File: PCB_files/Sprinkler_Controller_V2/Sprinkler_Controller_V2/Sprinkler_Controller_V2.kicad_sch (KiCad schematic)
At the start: 42 parts, among them J1 Screw_Terminal_01x02, J2 Screw_Terminal_01x11, U1 ESP32_DevKit_V1_DOIT, U12 TPP362081-T6TR

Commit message: V2 PCB Complete
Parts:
- added SW1: SW_SPST, Connector_PinHeader_2.54mm:PinHeader_1x02_P2.54mm_Vertical, symbol Switch:SW_SPST
- L1: footprint (none) -> Inductor_SMD:L_Vishay_IHLP-5050
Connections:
- net AC: now also SW1.2 (B); no longer J1.1 (Pin_1)
- new net AC_to_SW: J1.1 (Pin_1), SW1.1 (A)
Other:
- moved on the sheet: J1
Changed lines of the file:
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@@
 	)
 	(junction
-		(at 20.32 22.86)
-		(diameter 0)
-		(color 0 0 0 0)
-	)
-	(junction
 		(at 45.72 27.94)
 		(diameter 0)
@@
 	)
 	(junction
+		(at 25.4 27.94)
+		(diameter 0)
+		(color 0 0 0 0)
+	)
+	(junction
 		(at 35.56 43.18)
 		(diameter 0)
@@
 	(wire
 		(pts
+			(xy 19.05 22.86) (xy 19.05 25.4)
+		)
+		(stroke
+			(width 0)
+			(type default)
+		)
+	)
+	(wire
+		(pts
 			(xy 146.05 109.22) (xy 146.05 96.52)
 		)
@@
 	(wire
 		(pts
-			(xy 12.7 15.24) (xy 12.7 29.21)
+			(xy 12.7 15.24) (xy 12.7 40.64)
 		)
 		(stroke
@@
 	(wire
 		(pts
+			(xy 20.32 24.13) (xy 24.13 24.13)
+		)
+		(stroke
+			(width 0)
+			(type default)
+		)
+	)
+	(wire
+		(pts
 			(xy 153.67 129.54) (xy 175.26 129.54)
 		)
@@
 	(wire
 		(pts
+			(xy 20.32 22.86) (xy 20.32 24.13)
+		)
+		(stroke
+			(width 0)
+			(type default)
+		)
+	)
+	(wire
+		(pts
 			(xy 146.05 125.73) (xy 156.21 125.73)
 		)
@@
 	(wire
 		(pts
+			(xy 19.05 25.4) (xy 15.24 25.4)
+		)
+		(stroke
+			(width 0)
+			(type default)
+		)
+	)
+	(wire
+		(pts
 			(xy 219.71 99.06) (xy 219.71 158.75)
 		)
@@
 	(wire
 		(pts
+			(xy 19.05 20.32) (xy 20.32 20.32)
+		)
+		(stroke
+			(width 0)
+			(type default)
+		)
+	)
+	(wire
+		(pts
 			(xy 243.84 93.98) (xy 214.63 93.98)
 		)
@@
 	(wire
 		(pts
+			(xy 24.13 26.67) (xy 25.4 26.67)
+		)
+		(stroke
+			(width 0)
+			(type default)
+		)
+	)
+	(wire
+		(pts
 			(xy 151.13 21.59) (xy 153.67 21.59)
 		)
@@
 	(wire
 		(pts
+			(xy 24.13 24.13) (xy 24.13 26.67)
+		)
+		(stroke
+			(width 0)
+			(type default)
+		)
+	)
+	(wire
+		(pts
 			(xy 133.35 109.22) (xy 146.05 109.22)
 		)
@@
 	(wire
 		(pts
+			(xy 15.24 25.4) (xy 15.24 27.94)
+		)
+		(stroke
+			(width 0)
+			(type default)
+		)
+	)
+	(wire
+		(pts
 			(xy 153.67 115.57) (xy 153.67 129.54)
 		)
@@
 	(wire
 		(pts
+			(xy 25.4 26.67) (xy 25.4 27.94)
+		)
+		(stroke
+			(width 0)
+			(type default)
+		)
+	)
+	(wire
+		(pts
 			(xy 209.55 86.36) (xy 209.55 83.82)
 		)
@@
 	(wire
 		(pts
-			(xy 20.32 29.21) (xy 20.32 22.86)
-		)
-		(stroke
-			(width 0)
-			(type default)
-		)
-	)
-	(wire
-		(pts
 			(xy 109.22 121.92) (xy 109.22 119.38)
 		)
@@
 	(wire
 		(pts
+			(xy 25.4 27.94) (xy 25.4 40.64)
+		)
+		(stroke
+			(width 0)
+			(type default)
+		)
+	)
+	(wire
+		(pts
 			(xy 43.18 43.18) (xy 48.26 43.18)
 		)
@@
 	(wire
 		(pts
-			(xy 12.7 29.21) (xy 20.32 29.21)
+			(xy 12.7 40.64) (xy 25.4 40.64)
 		)
 		(stroke
@@
 		)
 	)
+	(global_label "AC_to_SW"
+		(shape input)
+		(at 15.24 27.94 270)
+		(fields_autoplaced yes)
+		(effects
+			(font
+				(size 1.27 1.27)
+			)
+			(justify right)
+		)
+		(property "Intersheetrefs" "${INTERSHEET_REFS}"
+			(at 15.24 39.7546 90)
+			(effects
+				(font
+					(size 1.27 1.27)
+				)
+				(justify right)
+				(hide yes)
+			)
+		)
+	)
 	(global_label "FB"
 		(shape input)
@@
 	)
 	(symbol
+		(lib_id "Switch:SW_SPST")
+		(at 20.32 27.94 0)
+		(unit 1)
+		(exclude_from_sim no)
+		(in_bom yes)
+		(on_board yes)
+		(dnp no)
+		(property "Reference" "SW1"
+			(at 18.034 25.4 0)
+			(effects
+				(font
+					(size 1.27 1.27)
+				)
+			)
+		)
+		(property "Value" "SW_SPST"
+			(at 20.32 30.48 0)
+			(effects
+				(font
+					(size 1.27 1.27)
+				)
+			)
+		)
+		(property "Footprint" "Connector_PinHeader_2.54mm:PinHeader_1x02_P2.54mm_Vertical"
+			(at 20.32 27.94 0)
+			(effects
+				(font
+					(size 1.27 1.27)
+				)
+				(hide yes)
+			)
+		)
+		(property "Datasheet" "~"
+			(at 20.32 27.94 0)
+			(effects
+				(font
+					(size 1.27 1.27)
+				)
+				(hide yes)
+			)
+		)
+		(property "Description" "Single Pole Single Throw (SPST) switch"
+			(at 20.32 27.94 0)
+			(effects
+				(font
+					(size 1.27 1.27)
+				)
+				(hide yes)
+			)
+		)
+		(pin "1"
+		)
+		(pin "2"
+		)
+		(instances
+			(project ""
+				(path "/4ebb9756-e934-4387-ad3a-d5db36981b1a"
+					(reference "SW1")
+					(unit 1)
+				)
+			)
+		)
+	)
+	(symbol
 		(lib_id "Device:LED")
 		(at 160.02 49.53 180)
@@
 			)
 		)
-		(property "Footprint" ""
+		(property "Footprint" "Inductor_SMD:L_Vishay_IHLP-5050"
 			(at 39.37 43.18 0)
 			(effects
@@
 	(symbol
 		(lib_id "Connector:Screw_Terminal_01x02")
-		(at 15.24 22.86 180)
+		(at 13.97 22.86 180)
 		(unit 1)
 		(exclude_from_sim no)
@@
 		(dnp no)
 		(property "Reference" "J1"
-			(at 16.002 26.162 0)
+			(at 14.732 26.162 0)
 			(effects
 				(font
@@
 		)
 		(property "Value" "Screw_Terminal_01x02"
-			(at 35.052 15.748 0)
+			(at 33.782 15.748 0)
 			(effects
 				(font
@@
 		)
 		(property "Footprint" "TerminalBlock_MetzConnect:TerminalBlock_MetzConnect_Type094_RT03502HBLU_1x02_P5.00mm_Horizontal"
-			(at 15.24 22.86 0)
+			(at 13.97 22.86 0)
 			(effects
 				(font
@@
 		)
 		(property "Datasheet" "~"
-			(at 15.24 22.86 0)
+			(at 13.97 22.86 0)
 			(effects
 				(font
@@
 		)
 		(property "Description" "Generic screw terminal, single row, 01x02, script generated (kicad-library-utils/schlib/autogen/connector/)"
-			(at 15.24 22.86 0)
+			(at 13.97 22.86 0)
 			(effects
 				(font

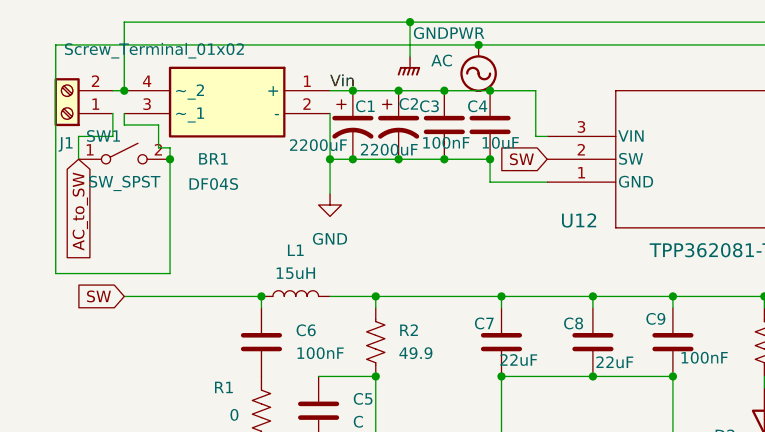
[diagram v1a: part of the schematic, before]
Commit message: changed C1,C2 capacitor values
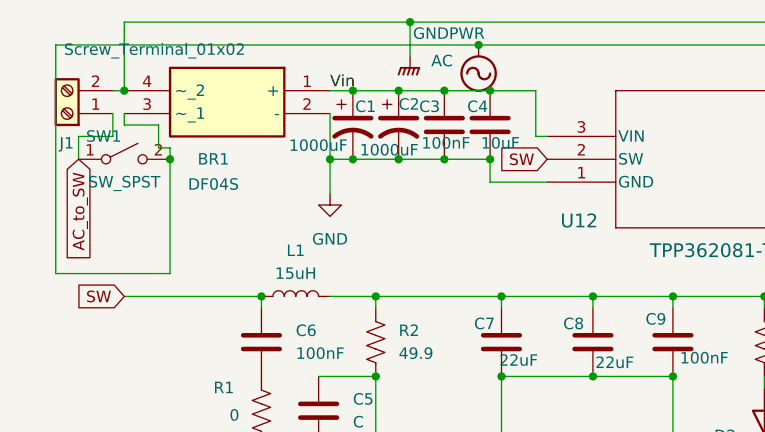
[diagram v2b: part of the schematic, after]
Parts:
- C1, C2: value 2200uF -> 1000uF
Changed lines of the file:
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@@
 			)
 		)
-		(property "Value" "2200uF"
+		(property "Value" "1000uF"
 			(at 46.482 26.924 0)
 			(effects
@@
 			)
 		)
-		(property "Value" "2200uF"
+		(property "Value" "1000uF"
 			(at 38.608 26.416 0)
 			(effects

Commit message: updated size of leds on pcb
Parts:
- D10, D11, D12, D3, D4, D5, D6, D7, D8, D9: footprint LED_SMD:LED_0402_1005Metric -> LED_SMD:LED_0805_2012Metric_Pad1.15x1.40mm_HandSolder
- D2: footprint LED_SMD:LED_0402_1005Metric -> LED_SMD:LED_0805_2012Metric
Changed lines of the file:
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@@
 	(label "Vin"
 		(at 43.18 20.32 0)
-		(fields_autoplaced yes)
 		(effects
 			(font
@@
 			)
 		)
-		(property "Footprint" "LED_SMD:LED_0402_1005Metric"
+		(property "Footprint" "LED_SMD:LED_0805_2012Metric_Pad1.15x1.40mm_HandSolder"
 			(at 158.75 154.94 0)
 			(effects
@@
 			)
 		)
-		(property "Footprint" "LED_SMD:LED_0402_1005Metric"
+		(property "Footprint" "LED_SMD:LED_0805_2012Metric"
 			(at 91.44 57.15 0)
 			(effects
@@
 			)
 		)
-		(property "Footprint" "LED_SMD:LED_0402_1005Metric"
+		(property "Footprint" "LED_SMD:LED_0805_2012Metric_Pad1.15x1.40mm_HandSolder"
 			(at 160.02 96.52 0)
 			(effects
@@
 			)
 		)
-		(property "Footprint" "LED_SMD:LED_0402_1005Metric"
+		(property "Footprint" "LED_SMD:LED_0805_2012Metric_Pad1.15x1.40mm_HandSolder"
 			(at 165.1 35.56 0)
 			(effects
@@
 			)
 		)
-		(property "Footprint" "LED_SMD:LED_0402_1005Metric"
+		(property "Footprint" "LED_SMD:LED_0805_2012Metric_Pad1.15x1.40mm_HandSolder"
 			(at 162.56 64.77 0)
 			(effects
@@
 			)
 		)
-		(property "Footprint" "LED_SMD:LED_0402_1005Metric"
+		(property "Footprint" "LED_SMD:LED_0805_2012Metric_Pad1.15x1.40mm_HandSolder"
 			(at 160.02 49.53 0)
 			(effects
@@
 			)
 		)
-		(property "Footprint" "LED_SMD:LED_0402_1005Metric"
+		(property "Footprint" "LED_SMD:LED_0805_2012Metric_Pad1.15x1.40mm_HandSolder"
 			(at 160.02 140.97 0)
 			(effects
@@
 			)
 		)
-		(property "Footprint" "LED_SMD:LED_0402_1005Metric"
+		(property "Footprint" "LED_SMD:LED_0805_2012Metric_Pad1.15x1.40mm_HandSolder"
 			(at 160.02 125.73 0)
 			(effects
@@
 			)
 		)
-		(property "Footprint" "LED_SMD:LED_0402_1005Metric"
+		(property "Footprint" "LED_SMD:LED_0805_2012Metric_Pad1.15x1.40mm_HandSolder"
 			(at 162.56 80.01 0)
 			(effects
@@
 			)
 		)
-		(property "Footprint" "LED_SMD:LED_0402_1005Metric"
+		(property "Footprint" "LED_SMD:LED_0805_2012Metric_Pad1.15x1.40mm_HandSolder"
 			(at 161.29 111.76 0)
 			(effects
@@
 			)
 		)
-		(property "Footprint" "LED_SMD:LED_0402_1005Metric"
+		(property "Footprint" "LED_SMD:LED_0805_2012Metric_Pad1.15x1.40mm_HandSolder"
 			(at 157.48 21.59 0)
 			(effects
